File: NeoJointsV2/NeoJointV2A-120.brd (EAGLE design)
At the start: 16.9 x 17 mm, 6 parts

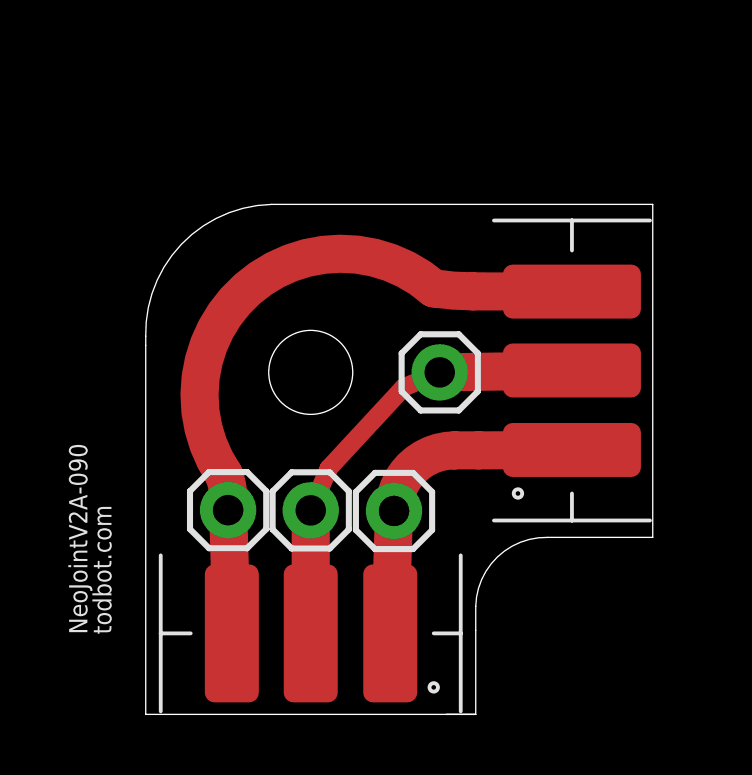
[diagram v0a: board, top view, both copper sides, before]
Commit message: layout fixes for 000,090,120
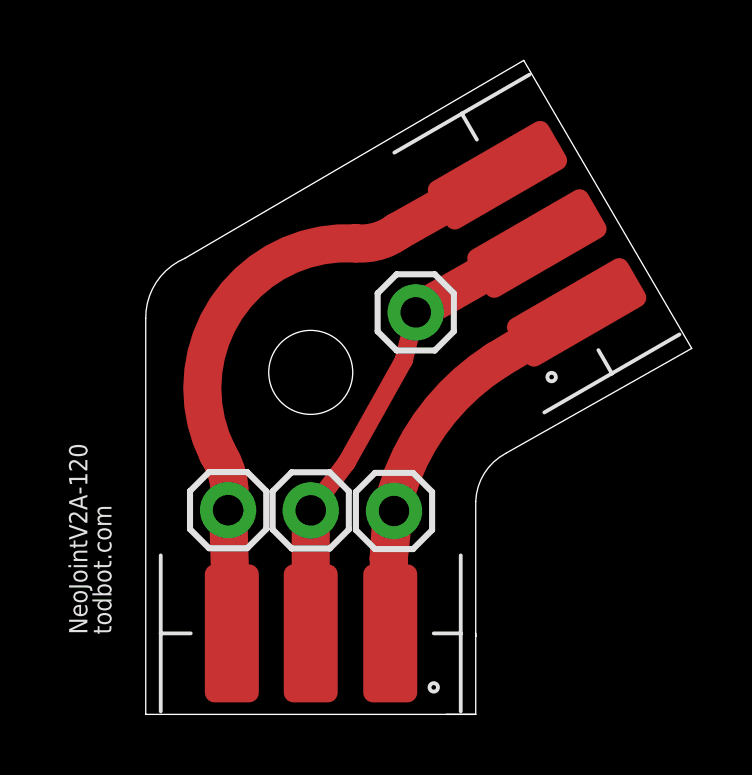
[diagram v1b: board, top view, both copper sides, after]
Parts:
- moved U$2 4.39 mm to (13.0, 15.7), turned to 30 degrees
- moved JP2 2.15 mm to (9.00, 13.4)
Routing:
- net A: track 10.8 -> 14.9 mm
- net B: track 15.0 -> 16.3 mm
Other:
- board size 16.9 x 17 mm -> 18.2 x 21.8 mm
- board text added: "NeoJointV2A-120"
- board text removed: "NeoJointV2A-090"
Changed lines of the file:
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@@
 <board>
 <plain>
-<text x="-1.945" y="2.667" size="0.6096" layer="21" rot="R90">NeoJointV2A-090</text>
+<text x="-1.945" y="2.667" size="0.6096" layer="21" rot="R90">NeoJointV2A-120</text>
 <wire x1="0" y1="0" x2="10.033" y2="0" width="0.0254" layer="20"/>
 <wire x1="10.033" y1="0" x2="11" y2="0" width="0.0254" layer="20"/>
-<wire x1="0" y1="0" x2="0" y2="12.3" width="0.0254" layer="20"/>
+<wire x1="0" y1="0" x2="0" y2="13.2" width="0.0254" layer="20"/>
 <hole x="5.5" y="11.4" drill="2.8"/>
 <text x="-1.143" y="2.667" size="0.6096" layer="21" rot="R90">todbot.com</text>
@@
 <wire x1="0.5" y1="18.9" x2="0.5" y2="-0.5" width="0" layer="48" style="longdash"/>
 <wire x1="11" y1="18.9" x2="11" y2="-0.5" width="0" layer="48" style="longdash"/>
-<wire x1="0" y1="12.3" x2="0" y2="12.6" width="0.0254" layer="20"/>
-<wire x1="0" y1="12.6" x2="4.2" y2="17" width="0.0254" layer="20" curve="-90"/>
-<wire x1="4.2" y1="17" x2="16.9" y2="17" width="0.0254" layer="20"/>
-<wire x1="16.9" y1="17" x2="16.9" y2="5.9" width="0.0254" layer="20"/>
-<wire x1="11" y1="2.8" x2="11" y2="0" width="0.0254" layer="20"/>
-<wire x1="11" y1="2.8" x2="11" y2="3.6" width="0.0254" layer="20"/>
-<wire x1="11" y1="3.6" x2="13.4" y2="5.9" width="0.0254" layer="20" curve="-90"/>
-<wire x1="13.4" y1="5.9" x2="16.9" y2="5.9" width="0.0254" layer="20"/>
-<wire x1="-2.382340625" y1="19.440915625" x2="14.588225" y2="2.070353125" width="0.002540625" layer="48" style="dashdot"/>
-<wire x1="17.739025" y1="4.33738125" x2="-3.045578125" y2="16.337375" width="0.002540625" layer="48" style="dashdot"/>
+<wire x1="0" y1="13.2" x2="1.3" y2="15.2" width="0.0254" layer="20" curve="-67.380135"/>
+<wire x1="1.3" y1="15.2" x2="12.6" y2="21.8" width="0.0254" layer="20"/>
+<wire x1="12.6" y1="21.8" x2="18.2" y2="12.2" width="0.0254" layer="20"/>
+<wire x1="11" y1="2.7" x2="11" y2="2.6" width="0.0254" layer="20"/>
+<wire x1="11" y1="2.6" x2="11" y2="0" width="0.0254" layer="20"/>
+<wire x1="18.2" y1="12.2" x2="12" y2="8.7" width="0.0254" layer="20"/>
+<wire x1="12" y1="8.7" x2="11" y2="7.1" width="0.0254" layer="20" curve="60"/>
+<wire x1="-2.382340625" y1="19.440915625" x2="14.588225" y2="2.070353125" width="0" layer="48" style="dashdot"/>
+<wire x1="11" y1="2.6" x2="11" y2="7.1" width="0.0254" layer="20"/>
 <wire x1="5.48445625" y1="23.618178125" x2="5.484459375" y2="-0.7818125" width="0" layer="48" style="dashdot"/>
 <circle x="5.5" y="11.4" radius="8.700571875" width="0.0254" layer="48"/>
-<wire x1="18.1" y1="17" x2="-2.9" y2="17" width="0" layer="48" style="dashdot"/>
-<wire x1="18.8" y1="11.4" x2="-4.2" y2="11.4" width="0" layer="48" style="dashdot"/>
-<wire x1="19.3" y1="5.9" x2="-3.7" y2="5.9" width="0" layer="48" style="dashdot"/>
+<wire x1="16.4" y1="17.4" x2="-2.6" y2="17.4" width="0" layer="48" style="dashdot"/>
+<wire x1="18.8" y1="11.4" x2="-5.2" y2="11.4" width="0" layer="48" style="dashdot"/>
+<wire x1="-3.390896875" y1="6.2535875" x2="17.3937125" y2="18.2535875" width="0" layer="48" style="dashdot"/>
+<wire x1="-5.590896875" y1="11.2535875" x2="15.1937125" y2="23.2535875" width="0" layer="48" style="dashdot"/>
+<wire x1="0.509103125" y1="2.0535875" x2="21.2937125" y2="14.0535875" width="0" layer="48" style="dashdot"/>
 </plain>
 <attributes>
@@
 <attribute name="VALUE" x="7.006" y="3.605" size="1.27" layer="27"/>
 </element>
-<element name="JP2" library="SparkFun-Connectors" package="1X01" value="" x="9.8" y="11.4" smashed="yes">
-<attribute name="VALUE" x="8.53" y="8.225" size="1.27" layer="27"/>
+<element name="JP2" library="SparkFun-Connectors" package="1X01" value="" x="9" y="13.4" smashed="yes">
+<attribute name="VALUE" x="7.73" y="10.225" size="1.27" layer="27"/>
 </element>
 <element name="JP3" library="SparkFun-Connectors" package="1X01" value="" x="2.746" y="6.808" smashed="yes">
@@
 </element>
 <element name="U$1" library="todstuff" package="LEDSTRIP-3P" value="LED_STRIP_3P" x="5.5" y="2.7" rot="R90"/>
-<element name="U$2" library="todstuff" package="LEDSTRIP-3P" value="LED_STRIP_3P" x="14.207246875" y="11.462865625"/>
+<element name="U$2" library="todstuff" package="LEDSTRIP-3P" value="LED_STRIP_3P" x="13.038240625" y="15.694671875" rot="R30"/>
 <element name="JP4" library="SparkFun-Connectors" package="1X01" value="" x="5.5" y="6.8" smashed="yes">
 <attribute name="VALUE" x="4.23" y="3.625" size="1.27" layer="27"/>
@@
 <contactref element="U$1" pad="A"/>
 <contactref element="U$2" pad="A"/>
-<wire x1="14.207246875" y1="8.812865625" x2="11.1" y2="8.8" width="1.27" layer="1"/>
-<wire x1="11.1" y1="8.8" x2="10.296" y2="8.8" width="1.27" layer="1"/>
-<wire x1="10.296" y1="8.8" x2="8.276" y2="6.78" width="1.27" layer="1" curve="90"/>
-<wire x1="8.15" y1="2.7" x2="8.276" y2="6.78" width="1.27" layer="1"/>
+<wire x1="14.363240625" y1="13.399703125" x2="11.7" y2="11.8" width="1.27" layer="1"/>
+<wire x1="8.15" y1="2.7" x2="8.1" y2="5.2" width="1.27" layer="1"/>
+<wire x1="8.276" y1="6.78" x2="8.1" y2="5.2" width="1.27" layer="1"/>
+<wire x1="8.1" y1="5.2" x2="8.2" y2="6.8" width="1.27" layer="1"/>
+<wire x1="8.2" y1="6.8" x2="11.7" y2="11.8" width="1.27" layer="1" curve="-45"/>
 </signal>
 <signal name="C">
@@
 <wire x1="2.87" y1="2.7" x2="2.746" y2="6.808" width="1.27" layer="1"/>
 <wire x1="2.746" y1="6.808" x2="2.6" y2="7" width="1.27" layer="1" curve="14.063416"/>
-<wire x1="14.207246875" y1="14.092865625" x2="10.9" y2="14.1" width="1.27" layer="1"/>
-<wire x1="2.746" y1="6.808" x2="2.7" y2="6.7" width="1.27" layer="1"/>
-<wire x1="2.7" y1="6.7" x2="2.6" y2="8" width="1.27" layer="1" curve="34.468853"/>
-<wire x1="2.6" y1="8" x2="9.6" y2="14.2" width="1.27" layer="1" curve="-165"/>
-<wire x1="10.9" y1="14.1" x2="9.6" y2="14.2" width="1.27" layer="1" curve="-8.550024"/>
+<wire x1="11.723240625" y1="17.972315625" x2="8.4" y2="16.1" width="1.27" layer="1"/>
+<wire x1="8.4" y1="16.1" x2="7" y2="15.7" width="1.27" layer="1" curve="-41.301553"/>
+<wire x1="7" y1="15.7" x2="2.4" y2="8.7" width="1.27" layer="1" curve="120"/>
+<wire x1="2.4" y1="8.7" x2="2.746" y2="6.808" width="1.27" layer="1" curve="-44.910296"/>
 </signal>
 <signal name="B">
@@
 <contactref element="JP4" pad="1"/>
 <wire x1="5.5" y1="2.7" x2="5.5" y2="6.8" width="1.27" layer="1"/>
-<wire x1="9.8" y1="11.4" x2="8.6" y2="10.9" width="0.6096" layer="1"/>
-<wire x1="8.6" y1="10.9" x2="6.1" y2="8.2" width="0.6096" layer="1"/>
-<wire x1="6.1" y1="8.2" x2="5.5" y2="6.8" width="0.6096" layer="1"/>
-<wire x1="14.207246875" y1="11.462865625" x2="9.8" y2="11.4" width="1.27" layer="1"/>
+<wire x1="9" y1="13.4" x2="13.038240625" y2="15.694671875" width="1.27" layer="1"/>
+<wire x1="5.5" y1="6.8" x2="6.7" y2="8.4" width="0.6096" layer="1"/>
+<wire x1="6.7" y1="8.4" x2="8.6" y2="11.8" width="0.6096" layer="1"/>
+<wire x1="8.6" y1="11.8" x2="9" y2="13.4" width="0.6096" layer="1"/>
 </signal>
 </signals>
